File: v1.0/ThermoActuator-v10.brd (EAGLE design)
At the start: 99.1 x 80 mm, 74 parts, among them IC1 ULN2003AD, IC2 LM358D, IC3 LM358D, IC4 LM358D, IC5 LM358D

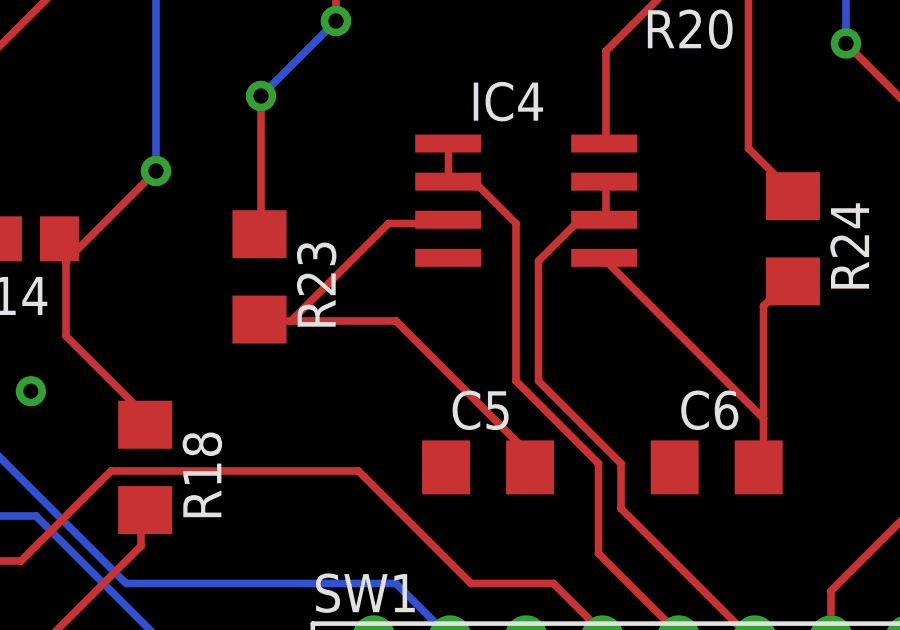
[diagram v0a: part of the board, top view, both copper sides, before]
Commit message: Nasty routing error fixed
The CH5 and CH6 did not work. That was because of one
unobserved airwire. The ground was not routed to the IC4. Too bad
On the boards the airwire must be mounted connecting the ground on C5
with the pin 4 of the IC4

The .brd is updated with one extra via, but because the boards are
already manufactured, there is nothing that can be redone. Solder a
wire...
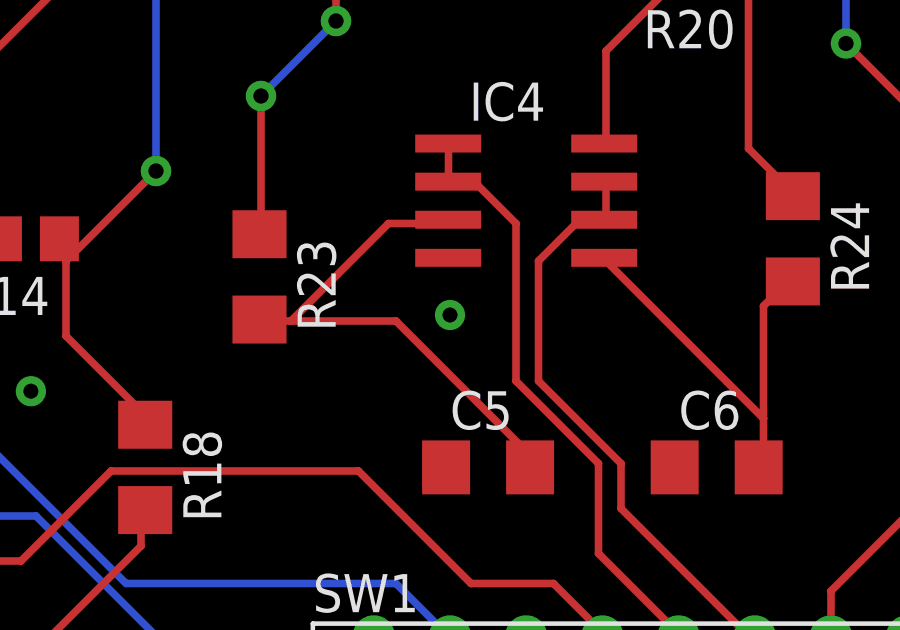
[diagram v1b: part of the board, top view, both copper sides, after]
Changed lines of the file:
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@@
 <via x="7.62" y="8.89" extent="1-16" drill="0.5" shape="octagon"/>
 <via x="67.31" y="8.89" extent="1-16" drill="0.5" shape="octagon"/>
-<wire x1="50.74" y1="46.355" x2="50.67" y2="39.37" width="0" layer="19" extent="1-1"/>
+<via x="50.8" y="44.45" extent="1-16" drill="0.5" shape="octagon"/>
 </signal>
 <signal name="VIN">
